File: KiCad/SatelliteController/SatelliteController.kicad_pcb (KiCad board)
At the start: 2 copper layers, 150 x 100 mm, 136 parts, among them J1 CONN_ICSP, J15 CONN_RS485, J2 CONN_USB, J3 USB_B_Micro, J4 DC_IN, J5 TO_CONVERTER, J6 FROM_CONVERTER, J7 CONN_STATUS_PANEL, J8 CONN_PANEL_BAORD_2, Q1 TJ8S06M3L, Q2 TJ8S06M3L, Q3 2SC3325-Y, SW1 SW_Push, SW11 SW_Push, SW17 SW_Push, SW18 SW_Push, SW19 SW_Push, SW2 SW_Push, SW20 SW_Push, SW21 SW_Push, SW22 SW_Push, SW23 SW_Push, SW24 SW_Push, SW25 SW_Push, U1 FT232RL, U2 ATMEGA2560-16AUR, U3 NJM7805SDL1, U4 INA219BIDCNT, U5 INA219BIDCNT, U8 LTC485CN8#PBF, Y1 HUSG-16.000-20

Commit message: 刻印を更新
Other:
- board text added: "Satellite Controller Build 1 Nov. 2023"
- board text removed: "Launch Controller Build 1 Sep. 2023"
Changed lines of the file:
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@@
     )
     (pad_to_mask_clearance 0)
-    (aux_axis_origin 47.633174 30.888716)
-    (grid_origin 69.6 87.8)
+    (aux_axis_origin 47.630705 30.846793)
+    (grid_origin 47.630705 30.846793)
     (pcbplotparams
       (layerselection 0x0000000_ffffffff)
@@
   (gr_line locked (start 47.630707 120.846793) (end 47.630707 40.846793)
     (stroke (width 0.1) (type default)) (layer "Edge.Cuts"))
-  (gr_arc locked (start 47.630707 40.846793) (mid 50.559639 33.775725) (end 57.630707 30.846793)
+  (gr_arc locked (start 47.630707 40.846793) (mid 50.559639 33.775726) (end 57.630707 30.846793)
     (stroke (width 0.1) (type default)) (layer "Edge.Cuts"))
   (gr_arc locked (start 197.630707 120.846793) (mid 194.701775 127.917861) (end 187.630707 130.846793)
@@
     (effects (font (size 1.5 1.5) (thickness 0.3) bold))
   )
-  (gr_text "Launch Controller\nBuild 1 Sep. 2023" (at 109.4 58.6) (layer "F.SilkS")
+  (gr_text "Satellite Controller\nBuild 1 Nov. 2023" (at 109.4 58.6) (layer "F.SilkS")
     (effects (font (size 1.5 1.5) (thickness 0.25) bold) (justify left bottom))
   )

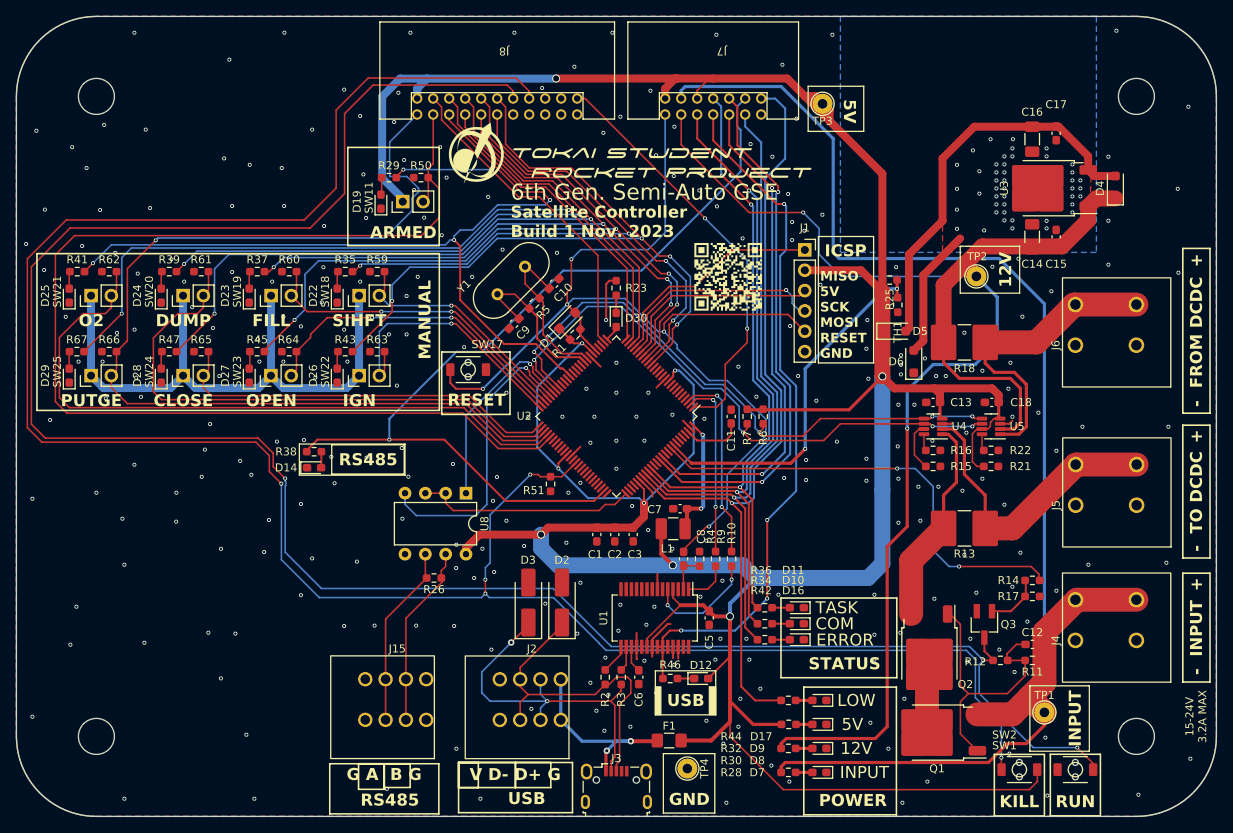
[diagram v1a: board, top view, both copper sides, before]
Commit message: 配線を避難させた
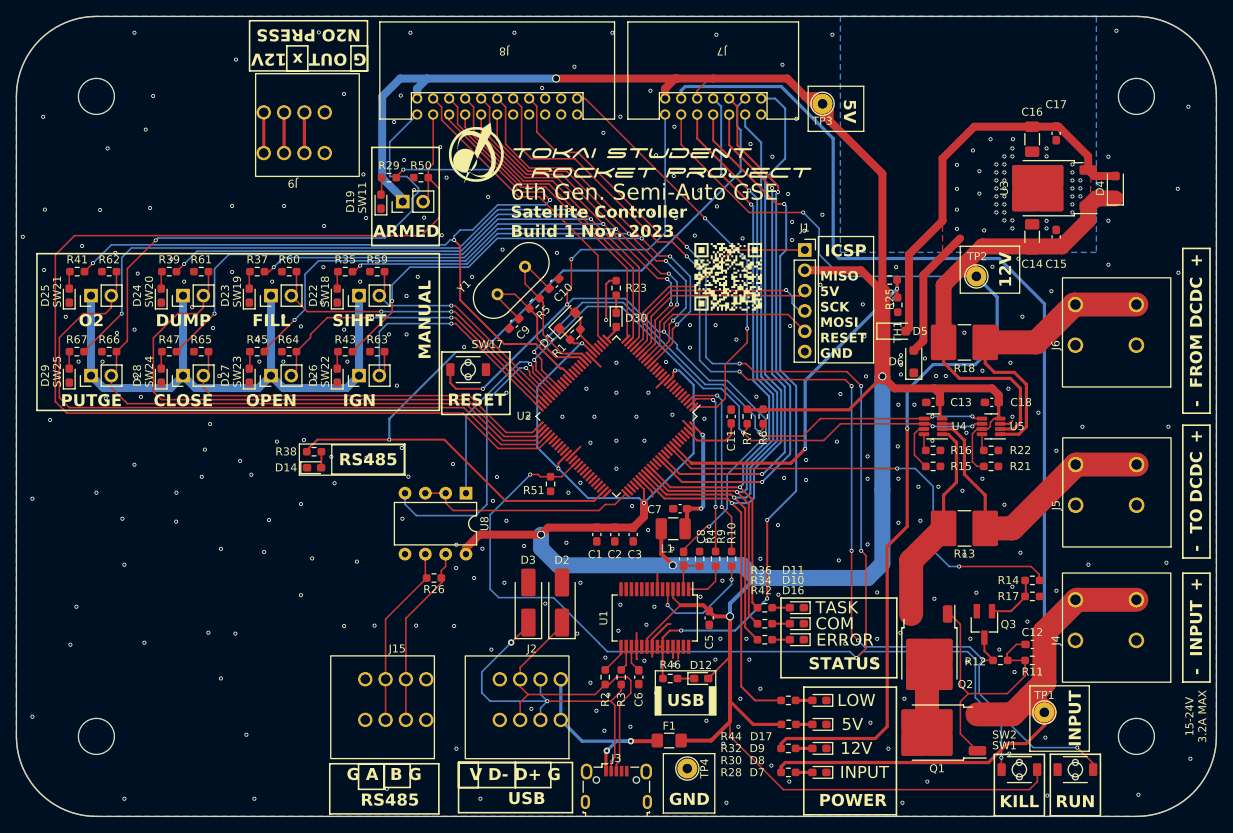
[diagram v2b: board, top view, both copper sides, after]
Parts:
- added J9: CONN_N2O_PRESS, TSRP_TerminalBlock_Alphaplus:TB401-1-4-E, F.Cu at (82.2, 47.9)
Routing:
- net CTL_RUN: track 261.6 -> 143.3 mm, vias 3 -> 7
- net CTL_KILL: track 277.0 -> 202.7 mm, vias 5 -> 7
- net CONN_LED_12V: track 187.1 -> 192.2 mm
- net unconnected-(J9-Pin_3-Pad3): track 0.00 -> 5.08 mm
- net VREF_N2O_PRESS: track 0.00 -> 5.08 mm
- net VREF_THERMISTOR: track 45.8 -> 44.9 mm
- net GND: vias 289 -> 294
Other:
- board text added: "G OUT x 12V"
- board text added: "N2O PRESS"

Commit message: N2O圧力計測回路を追加
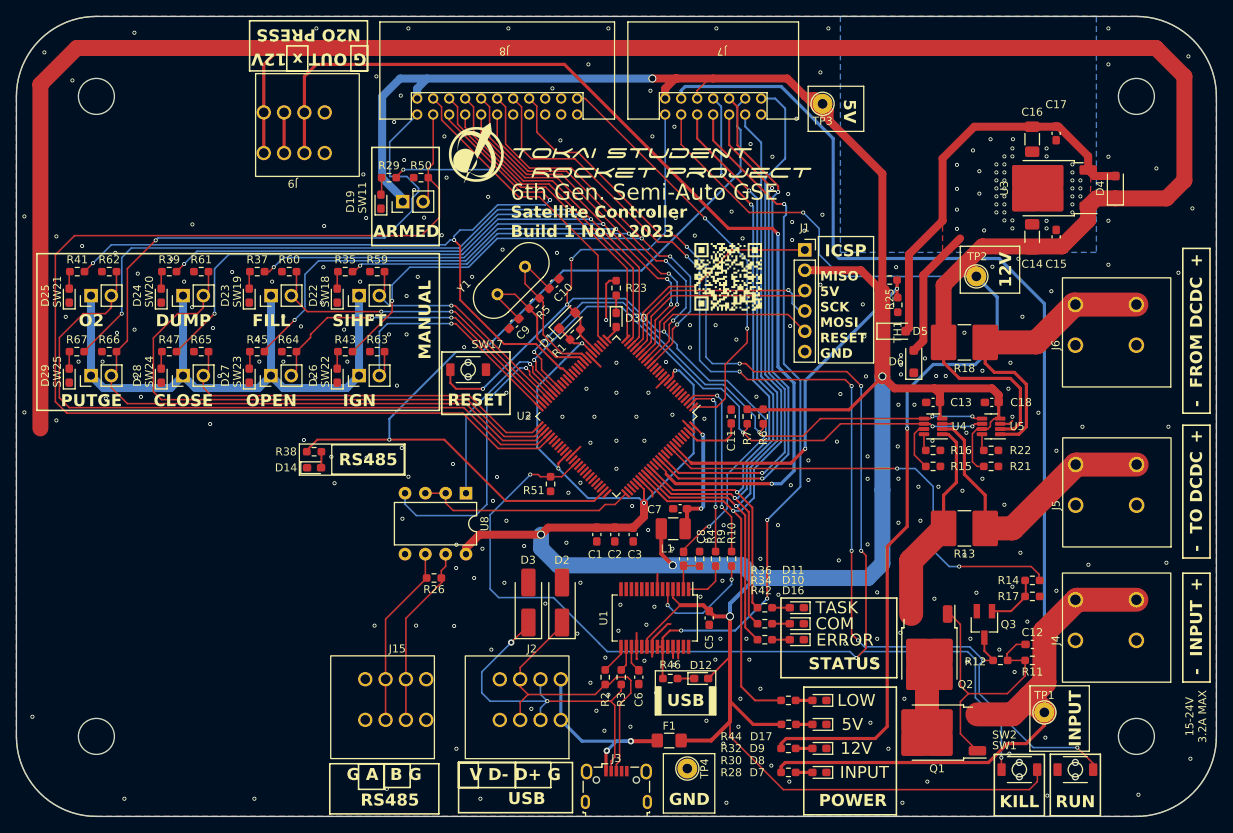
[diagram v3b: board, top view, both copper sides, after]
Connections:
- U2 pad 87: unconnected-(U2-PK2-Pad87) -> VREF_N2O_PRESS
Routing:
- net CONN_LED_12V: track 192.2 -> 413.0 mm
- net VREF_N2O_PRESS: track 5.08 -> 127.7 mm, vias 0 -> 2
- net GND: vias 294 -> 262

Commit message: サテコンのボード図を作成
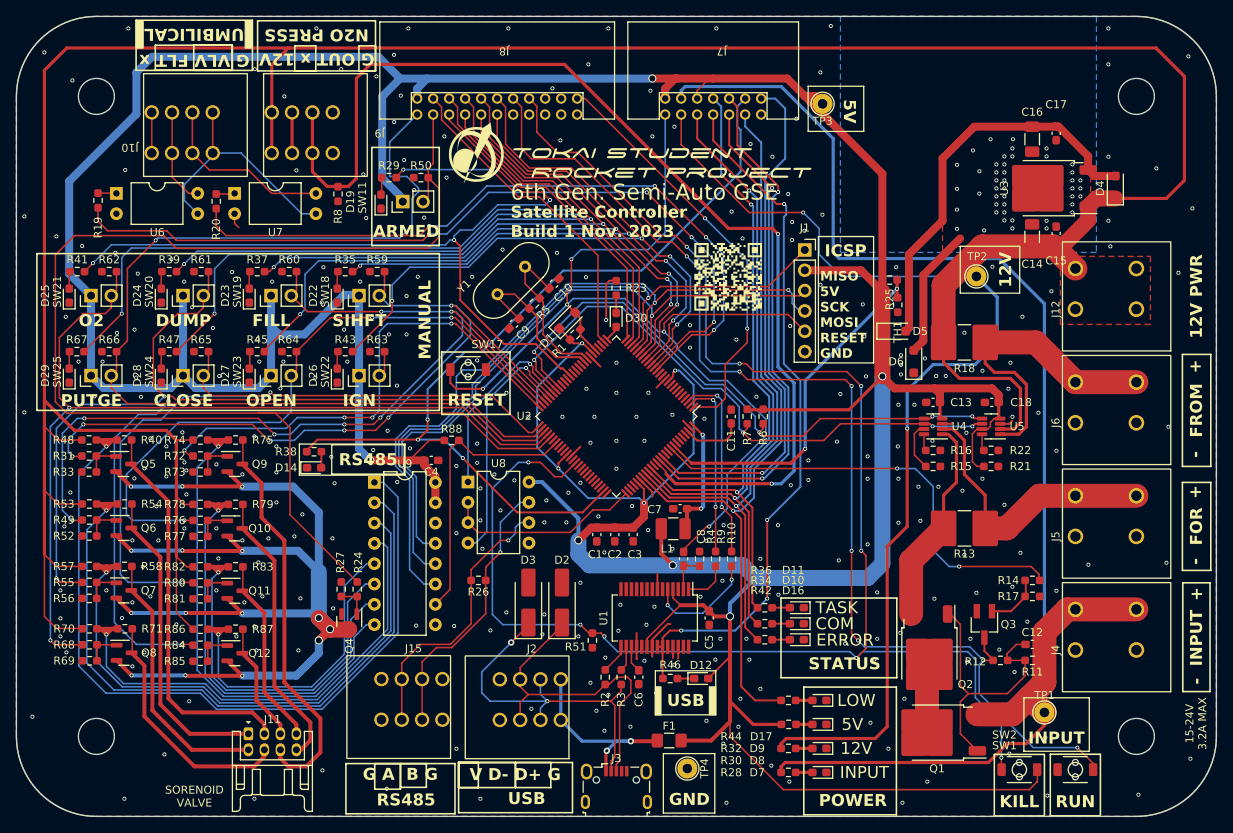
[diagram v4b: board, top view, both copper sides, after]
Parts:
- added C4: 0.1uF, Capacitor_SMD:C_0603_1608Metric_Pad1.08x0.95mm_HandSolder, F.Cu at (99.5, 86.3)
- added J10: CONN_UMBILICAL, TSRP_TerminalBlock_Alphaplus:TB401-1-4-E, F.Cu at (68.2, 47.9)
- added J11: CONN_SORENOID_VALVE, TSRP_Connector_Hirose:DF11B-8DP-2DS, F.Cu at (76.6, 120.5)
- added J12: RELAY_POWER, TSRP_TerminalBlock_Alphaplus:TB411-2-2-E-1, F.Cu at (182.6, 67.4)
- added Q10: AO3400A, Package_TO_SOT_SMD:SOT-23, F.Cu at (74.9, 94.8)
- added Q11: AO3400A, Package_TO_SOT_SMD:SOT-23, F.Cu at (74.9, 102.6)
- added Q12: AO3400A, Package_TO_SOT_SMD:SOT-23, F.Cu at (74.9, 110.4)
- added Q4: AO3400A, Package_TO_SOT_SMD:SOT-23, F.Cu at (89.2, 106.5)
- added Q5: AO3400A, Package_TO_SOT_SMD:SOT-23, F.Cu at (61.0, 86.8)
- added Q6: AO3400A, Package_TO_SOT_SMD:SOT-23, F.Cu at (61.1, 94.8)
- added Q7: AO3400A, Package_TO_SOT_SMD:SOT-23, F.Cu at (61.1, 102.6)
- added Q8: AO3400A, Package_TO_SOT_SMD:SOT-23, F.Cu at (61.1, 110.4)
- added Q9: AO3400A, Package_TO_SOT_SMD:SOT-23, F.Cu at (74.9, 86.8)
- added R19: 300R, Resistor_SMD:R_0603_1608Metric_Pad0.98x0.95mm_HandSolder, F.Cu at (57.8, 53.8)
- added R20: 300R, Resistor_SMD:R_0603_1608Metric_Pad0.98x0.95mm_HandSolder, F.Cu at (72.6, 54.0)
- added R24: 200R, Resistor_SMD:R_0603_1608Metric_Pad0.98x0.95mm_HandSolder, F.Cu at (90.2, 102.4)
- added R27: 10kR, Resistor_SMD:R_0603_1608Metric_Pad0.98x0.95mm_HandSolder, F.Cu at (88.2, 102.4)
- added R31: 200R, Resistor_SMD:R_0603_1608Metric_Pad0.98x0.95mm_HandSolder, F.Cu at (56.7, 85.8)
- added R33: 10kR, Resistor_SMD:R_0603_1608Metric_Pad0.98x0.95mm_HandSolder, F.Cu at (56.7, 87.8)
- added R40: 2kR, Resistor_SMD:R_0603_1608Metric_Pad0.98x0.95mm_HandSolder, F.Cu at (61.1, 83.8)
- added R48: 12kR, Resistor_SMD:R_0603_1608Metric_Pad0.98x0.95mm_HandSolder, F.Cu at (56.7, 83.8)
- added R49: 200R, Resistor_SMD:R_0603_1608Metric_Pad0.98x0.95mm_HandSolder, F.Cu at (56.8, 93.8)
- added R52: 10kR, Resistor_SMD:R_0603_1608Metric_Pad0.98x0.95mm_HandSolder, F.Cu at (56.8, 95.8)
- added R53: 12kR, Resistor_SMD:R_0603_1608Metric_Pad0.98x0.95mm_HandSolder, F.Cu at (56.8, 91.8)
- added R54: 2kR, Resistor_SMD:R_0603_1608Metric_Pad0.98x0.95mm_HandSolder, F.Cu at (61.2, 91.8)
- added R55: 200R, Resistor_SMD:R_0603_1608Metric_Pad0.98x0.95mm_HandSolder, F.Cu at (56.8, 101.6)
- added R56: 10kR, Resistor_SMD:R_0603_1608Metric_Pad0.98x0.95mm_HandSolder, F.Cu at (56.8, 103.6)
- added R57: 12kR, Resistor_SMD:R_0603_1608Metric_Pad0.98x0.95mm_HandSolder, F.Cu at (56.8, 99.6)
- added R58: 2kR, Resistor_SMD:R_0603_1608Metric_Pad0.98x0.95mm_HandSolder, F.Cu at (61.2, 99.6)
- added R68: 200R, Resistor_SMD:R_0603_1608Metric_Pad0.98x0.95mm_HandSolder, F.Cu at (56.8, 109.4)
- added R69: 10kR, Resistor_SMD:R_0603_1608Metric_Pad0.98x0.95mm_HandSolder, F.Cu at (56.8, 111.4)
- added R70: 12kR, Resistor_SMD:R_0603_1608Metric_Pad0.98x0.95mm_HandSolder, F.Cu at (56.8, 107.4)
- added R71: 2kR, Resistor_SMD:R_0603_1608Metric_Pad0.98x0.95mm_HandSolder, F.Cu at (61.2, 107.4)
- added R72: 200R, Resistor_SMD:R_0603_1608Metric_Pad0.98x0.95mm_HandSolder, F.Cu at (70.6, 85.8)
- added R73: 10kR, Resistor_SMD:R_0603_1608Metric_Pad0.98x0.95mm_HandSolder, F.Cu at (70.6, 87.8)
- added R74: 12kR, Resistor_SMD:R_0603_1608Metric_Pad0.98x0.95mm_HandSolder, F.Cu at (70.6, 83.8)
- added R75: 2kR, Resistor_SMD:R_0603_1608Metric_Pad0.98x0.95mm_HandSolder, F.Cu at (75.0, 83.8)
- added R76: 200R, Resistor_SMD:R_0603_1608Metric_Pad0.98x0.95mm_HandSolder, F.Cu at (70.6, 93.8)
- added R77: 10kR, Resistor_SMD:R_0603_1608Metric_Pad0.98x0.95mm_HandSolder, F.Cu at (70.6, 95.8)
- added R78: 12kR, Resistor_SMD:R_0603_1608Metric_Pad0.98x0.95mm_HandSolder, F.Cu at (70.6, 91.8)
- added R79: 2kR, Resistor_SMD:R_0603_1608Metric_Pad0.98x0.95mm_HandSolder, F.Cu at (75.0, 91.8)
- added R8: 240R, Resistor_SMD:R_0603_1608Metric_Pad0.98x0.95mm_HandSolder, F.Cu at (87.8, 53.0)
- added R80: 200R, Resistor_SMD:R_0603_1608Metric_Pad0.98x0.95mm_HandSolder, F.Cu at (70.6, 101.6)
- added R81: 10kR, Resistor_SMD:R_0603_1608Metric_Pad0.98x0.95mm_HandSolder, F.Cu at (70.6, 103.6)
- added R82: 12kR, Resistor_SMD:R_0603_1608Metric_Pad0.98x0.95mm_HandSolder, F.Cu at (70.6, 99.6)
- added R83: 2kR, Resistor_SMD:R_0603_1608Metric_Pad0.98x0.95mm_HandSolder, F.Cu at (75.0, 99.6)
- added R84: 200R, Resistor_SMD:R_0603_1608Metric_Pad0.98x0.95mm_HandSolder, F.Cu at (70.6, 109.4)
- added R85: 10kR, Resistor_SMD:R_0603_1608Metric_Pad0.98x0.95mm_HandSolder, F.Cu at (70.6, 111.4)
- added R86: 12kR, Resistor_SMD:R_0603_1608Metric_Pad0.98x0.95mm_HandSolder, F.Cu at (70.6, 107.4)
- added R87: 2kR, Resistor_SMD:R_0603_1608Metric_Pad0.98x0.95mm_HandSolder, F.Cu at (75.0, 107.4)
- added R88: 10kR, Resistor_SMD:R_0603_1608Metric_Pad0.98x0.95mm_HandSolder, F.Cu at (102.0, 83.8)
- added U6: TLP785F, Package_DIP:DIP-4_W10.16mm, F.Cu at (60.1, 53.0)
- added U7: TLP785F, Package_DIP:DIP-4_W10.16mm, F.Cu at (74.9, 53.0)
- added U9: MCP3208, Package_DIP:DIP-16_W7.62mm, F.Cu at (92.4, 89.1)
- moved R51 20.2 mm to (119.6, 108.8)
- moved J6 9.70 mm to (182.6, 81.6)
- moved R26 5.56 mm to (105.4, 101.3)
- moved J5 3.90 mm to (182.6, 95.8)
- moved J15 2.02 mm to (97.3, 113.7)
- moved U8 1.42 mm to (104.1, 89.0), turned to 0 degrees
- moved J4 1.20 mm to (182.6, 110.0)
- moved J9 1.00 mm to (83.2, 47.9)
- moved C15 0.42 mm to (177.6, 58.0)
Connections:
- U2 pad 14: unconnected-(U2-PH2-Pad14) -> VALVE_MODE
- U2 pad 15: unconnected-(U2-PH3-Pad15) -> FLIGHT_MODE
- U2 pad 57: unconnected-(U2-PC4-Pad57) -> CS_ADC
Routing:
- net SAFETY_12V: track 0.00 -> 144.1 mm, vias 0 -> 15
- net FLIGHT_MODE: track 0.00 -> 103.3 mm, vias 0 -> 4
- net VREF_SHIFT: track 0.00 -> 102.3 mm, vias 0 -> 1
- net CONN_LED_12V: track 413.0 -> 513.5 mm
- net VALVE_MODE: track 0.00 -> 91.3 mm, vias 0 -> 4
- net VREF_FILL: track 0.00 -> 88.9 mm, vias 0 -> 1
- net CONN_LED_5V: track 528.8 -> 615.7 mm, vias 9 -> 10
- net VREF_DUMP: track 0.00 -> 75.5 mm, vias 0 -> 1
- net CTL_FILL: track 40.4 -> 113.6 mm, vias 2 -> 7
- net VREF_IGNITOR: track 0.00 -> 66.3 mm, vias 0 -> 1
- net CTL_SHIFT: track 29.6 -> 95.4 mm, vias 1 -> 6
- net SPI_MOSI: track 27.1 -> 92.8 mm, vias 1 -> 2
- net VREF_O2: track 0.00 -> 63.0 mm, vias 0 -> 1
- net SPI_MISO: track 28.3 -> 88.1 mm, vias 0 -> 1
- net SPI_SCK: track 25.7 -> 83.0 mm, vias 0 -> 1
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- added copper zone on F.Cu, net CONN_LED_12V
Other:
- board text added: "12V PWR"
- board text added: "CONN_N2O_PRESS"
- board text added: "FOR"
- board text added: "FROM"
- board text added: "G VLV FLT x"
- board text added: "SORENOID VALVE"
- board text added: "UMBILICAL"
- board text removed: "FROM DCDC"
- board text removed: "TO DCDC"
